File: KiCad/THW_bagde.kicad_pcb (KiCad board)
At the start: 2 copper layers, 84.9 x 82.9 mm, 46 parts, among them J1 USB_B, J2 ISP, SW1 SW_Push, SW2 SW_Push, SW3 SW_Push, U1 ATmega328-P, Y1 Crystal

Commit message: first tests with tks-badge firmware
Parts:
- added C8: 100n, Capacitor_THT:C_Disc_D3.8mm_W2.6mm_P2.50mm, F.Cu at (158.2, 88.5)
- C3: value C -> 100n
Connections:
- R10 pad 1: /PC5 -> /PC4
- R6 pad 1: /PC1 -> /PC0
- R7 pad 1: /PC2 -> /PC1
- R8 pad 1: /PC3 -> /PC2
- R9 pad 1: /PC4 -> /PC3
- U1 pad 23: unconnected-(U1-Pad23) -> /PC0
- U1 pad 28: /PC5 -> unconnected-(U1-Pad28)
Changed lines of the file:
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@@
   (net 22 "/PC3")
   (net 23 "/PC4")
-  (net 24 "/PC5")
+  (net 24 "Net-(C6-Pad1)")
   (net 25 "unconnected-(U1-Pad11)")
   (net 26 "+5V")
@@
   (net 31 "unconnected-(U1-Pad16)")
   (net 32 "unconnected-(U1-Pad21)")
-  (net 33 "unconnected-(U1-Pad23)")
+  (net 33 "Net-(C7-Pad1)")
   (net 34 "Net-(F1-Pad1)")
-  (net 35 "Net-(SW3-Pad2)")
-  (net 36 "Net-(SW2-Pad2)")
+  (net 35 "/PC0")
+  (net 36 "unconnected-(U1-Pad28)")
   (net 37 "GND")
   (net 38 "/RES")
@@
       (net 37 "GND") (pintype "passive"))
     (pad "2" thru_hole oval (at 10.16 0) (size 1.6 1.6) (drill 0.8) (layers *.Cu *.Mask)
-      (net 36 "Net-(SW2-Pad2)") (pintype "passive"))
+      (net 24 "Net-(C6-Pad1)") (pintype "passive"))
     (model "${KICAD6_3DMODEL_DIR}/Resistor_THT.3dshapes/R_Axial_DIN0207_L6.3mm_D2.5mm_P10.16mm_Horizontal.wrl"
       (offset (xyz 0 0 0))
@@
     (fp_line (start 8.23 1.25) (end 8.23 -1.25) (layer "F.Fab") (width 0.1))
     (pad "1" thru_hole circle (at 0 0) (size 1.6 1.6) (drill 0.8) (layers *.Cu *.Mask)
-      (net 24 "/PC5") (pintype "passive"))
+      (net 23 "/PC4") (pintype "passive"))
     (pad "2" thru_hole oval (at 10.16 0) (size 1.6 1.6) (drill 0.8) (layers *.Cu *.Mask)
       (net 12 "Net-(D10-Pad2)") (pintype "passive"))
@@
       (net 37 "GND") (pintype "passive"))
     (pad "2" thru_hole oval (at 10.16 0) (size 1.6 1.6) (drill 0.8) (layers *.Cu *.Mask)
-      (net 35 "Net-(SW3-Pad2)") (pintype "passive"))
+      (net 33 "Net-(C7-Pad1)") (pintype "passive"))
     (model "${KICAD6_3DMODEL_DIR}/Resistor_THT.3dshapes/R_Axial_DIN0207_L6.3mm_D2.5mm_P10.16mm_Horizontal.wrl"
       (offset (xyz 0 0 0))
@@
     (fp_line (start 1.93 -1.25) (end 1.93 1.25) (layer "F.Fab") (width 0.1))
     (pad "1" thru_hole circle (at 0 0) (size 1.6 1.6) (drill 0.8) (layers *.Cu *.Mask)
-      (net 19 "/PC2") (pintype "passive"))
+      (net 18 "/PC1") (pintype "passive"))
     (pad "2" thru_hole oval (at 10.16 0) (size 1.6 1.6) (drill 0.8) (layers *.Cu *.Mask)
       (net 9 "Net-(D7-Pad2)") (pintype "passive"))
@@
       (net 26 "+5V") (pinfunction "1") (pintype "passive"))
     (pad "2" thru_hole circle (at 6.5 4.5 90) (size 2 2) (drill 1.1) (layers *.Cu *.Mask)
-      (net 35 "Net-(SW3-Pad2)") (pinfunction "2") (pintype "passive"))
+      (net 33 "Net-(C7-Pad1)") (pinfunction "2") (pintype "passive"))
     (pad "2" thru_hole circle (at 0 4.5 90) (size 2 2) (drill 1.1) (layers *.Cu *.Mask)
-      (net 35 "Net-(SW3-Pad2)") (pinfunction "2") (pintype "passive"))
+      (net 33 "Net-(C7-Pad1)") (pinfunction "2") (pintype "passive"))
     (model "${KICAD6_3DMODEL_DIR}/Button_Switch_THT.3dshapes/SW_PUSH_6mm.wrl"
       (offset (xyz 0 0 0))
@@
     (fp_line (start 8.23 -1.25) (end 1.93 -1.25) (layer "F.Fab") (width 0.1))
     (pad "1" thru_hole circle (at 0 0) (size 1.6 1.6) (drill 0.8) (layers *.Cu *.Mask)
-      (net 22 "/PC3") (pintype "passive"))
+      (net 19 "/PC2") (pintype "passive"))
     (pad "2" thru_hole oval (at 10.16 0) (size 1.6 1.6) (drill 0.8) (layers *.Cu *.Mask)
       (net 10 "Net-(D8-Pad2)") (pintype "passive"))
@@
     (fp_line (start -0.65 -1.3) (end -0.65 1.3) (layer "F.Fab") (width 0.1))
     (pad "1" thru_hole circle (at 0 0 270) (size 1.6 1.6) (drill 0.8) (layers *.Cu *.Mask)
-      (net 36 "Net-(SW2-Pad2)") (pintype "passive"))
+      (net 24 "Net-(C6-Pad1)") (pintype "passive"))
     (pad "2" thru_hole circle (at 2.5 0 270) (size 1.6 1.6) (drill 0.8) (layers *.Cu *.Mask)
       (net 37 "GND") (pintype "passive"))
@@
     (fp_line (start 0 0) (end 1.93 0) (layer "F.Fab") (width 0.1))
     (pad "1" thru_hole circle (at 0 0) (size 1.6 1.6) (drill 0.8) (layers *.Cu *.Mask)
-      (net 18 "/PC1") (pintype "passive"))
+      (net 35 "/PC0") (pintype "passive"))
     (pad "2" thru_hole oval (at 10.16 0) (size 1.6 1.6) (drill 0.8) (layers *.Cu *.Mask)
       (net 8 "Net-(D6-Pad2)") (pintype "passive"))
@@
   )
   (footprint "Capacitor_THT:C_Disc_D3.8mm_W2.6mm_P2.50mm" (layer "F.Cu")
+    (at 158.25 88.45 -90)
+    (descr "C, Disc series, Radial, pin pitch=2.50mm, , diameter*width=3.8*2.6mm^2, Capacitor, http://www.vishay.com/docs/45233/krseries.pdf")
+    (tags "C Disc series Radial pin pitch 2.50mm  diameter 3.8mm width 2.6mm Capacitor")
+    (property "Sheetfile" "THW_bagde.kicad_sch")
+    (property "Sheetname" "")
+    (attr through_hole)
+    (fp_text reference "C8" (at 4.3 0 180) (layer "F.SilkS")
+      (effects (font (size 1 1) (thickness 0.15)))
+    )
+    (fp_text value "100n" (at 1.25 2.55 90) (layer "F.Fab") hide
+      (effects (font (size 1 1) (thickness 0.15)))
+    )
+    (fp_text user "${REFERENCE}" (at 1.25 0 90) (layer "F.Fab") hide
+      (effects (font (size 0.76 0.76) (thickness 0.114)))
+    )
+    (fp_line (start -0.77 0.795) (end -0.77 1.42) (layer "F.SilkS") (width 0.12))
+    (fp_line (start 3.27 0.795) (end 3.27 1.42) (layer "F.SilkS") (width 0.12))
+    (fp_line (start -0.77 -1.42) (end 3.27 -1.42) (layer "F.SilkS") (width 0.12))
+    (fp_line (start -0.77 -1.42) (end -0.77 -0.795) (layer "F.SilkS") (width 0.12))
+    (fp_line (start -0.77 1.42) (end 3.27 1.42) (layer "F.SilkS") (width 0.12))
+    (fp_line (start 3.27 -1.42) (end 3.27 -0.795) (layer "F.SilkS") (width 0.12))
+    (fp_line (start 3.55 -1.55) (end -1.05 -1.55) (layer "F.CrtYd") (width 0.05))
+    (fp_line (start -1.05 -1.55) (end -1.05 1.55) (layer "F.CrtYd") (width 0.05))
+    (fp_line (start -1.05 1.55) (end 3.55 1.55) (layer "F.CrtYd") (width 0.05))
+    (fp_line (start 3.55 1.55) (end 3.55 -1.55) (layer "F.CrtYd") (width 0.05))
+    (fp_line (start 3.15 1.3) (end 3.15 -1.3) (layer "F.Fab") (width 0.1))
+    (fp_line (start -0.65 -1.3) (end -0.65 1.3) (layer "F.Fab") (width 0.1))
+    (fp_line (start 3.15 -1.3) (end -0.65 -1.3) (layer "F.Fab") (width 0.1))
+    (fp_line (start -0.65 1.3) (end 3.15 1.3) (layer "F.Fab") (width 0.1))
+    (pad "1" thru_hole circle (at 0 0 270) (size 1.6 1.6) (drill 0.8) (layers *.Cu *.Mask)
+      (net 26 "+5V") (pintype "passive"))
+    (pad "2" thru_hole circle (at 2.5 0 270) (size 1.6 1.6) (drill 0.8) (layers *.Cu *.Mask)
+      (net 37 "GND") (pintype "passive"))
+    (model "${KICAD6_3DMODEL_DIR}/Capacitor_THT.3dshapes/C_Disc_D3.8mm_W2.6mm_P2.50mm.wrl"
+      (offset (xyz 0 0 0))
+      (scale (xyz 1 1 1))
+      (rotate (xyz 0 0 0))
+    )
+  )
+  (footprint "Capacitor_THT:C_Disc_D3.8mm_W2.6mm_P2.50mm" (layer "F.Cu")
     (at 140.9246 87.503 180)
     (descr "C, Disc series, Radial, pin pitch=2.50mm, , diameter*width=3.8*2.6mm^2, Capacitor, http://www.vishay.com/docs/45233/krseries.pdf")
@@
       (effects (font (size 1 1) (thickness 0.15)))
     )
-    (fp_text value "C" (at 1.25 2.55) (layer "F.Fab") hide
+    (fp_text value "100n" (at 1.25 2.55) (layer "F.Fab") hide
       (effects (font (size 1 1) (thickness 0.15)))
     )
@@
       (net 37 "GND") (pinfunction "GND") (pintype "passive"))
     (pad "23" thru_hole oval (at 7.62 12.7) (size 1.6 1.6) (drill 0.8) (layers *.Cu *.Mask)
-      (net 33 "unconnected-(U1-Pad23)") (pinfunction "PC0") (pintype "bidirectional"))
+      (net 35 "/PC0") (pinfunction "PC0") (pintype "bidirectional"))
     (pad "24" thru_hole oval (at 7.62 10.16) (size 1.6 1.6) (drill 0.8) (layers *.Cu *.Mask)
       (net 18 "/PC1") (pinfunction "PC1") (pintype "bidirectional"))
@@
       (net 23 "/PC4") (pinfunction "PC4") (pintype "bidirectional"))
     (pad "28" thru_hole oval (at 7.62 0) (size 1.6 1.6) (drill 0.8) (layers *.Cu *.Mask)
-      (net 24 "/PC5") (pinfunction "PC5") (pintype "bidirectional"))
+      (net 36 "unconnected-(U1-Pad28)") (pinfunction "PC5") (pintype "bidirectional+no_connect"))
     (model "${KICAD6_3DMODEL_DIR}/Package_DIP.3dshapes/DIP-28_W7.62mm.wrl"
       (offset (xyz 0 0 4))
@@
     (fp_line (start -0.65 1.3) (end 3.15 1.3) (layer "F.Fab") (width 0.1))
     (pad "1" thru_hole circle (at 0 0 270) (size 1.6 1.6) (drill 0.8) (layers *.Cu *.Mask)
-      (net 35 "Net-(SW3-Pad2)") (pintype "passive"))
+      (net 33 "Net-(C7-Pad1)") (pintype "passive"))
     (pad "2" thru_hole circle (at 2.5 0 270) (size 1.6 1.6) (drill 0.8) (layers *.Cu *.Mask)
       (net 37 "GND") (pintype "passive"))
@@
       (net 26 "+5V") (pinfunction "1") (pintype "passive"))
     (pad "2" thru_hole circle (at 0 4.5 90) (size 2 2) (drill 1.1) (layers *.Cu *.Mask)
-      (net 36 "Net-(SW2-Pad2)") (pinfunction "2") (pintype "passive"))
+      (net 24 "Net-(C6-Pad1)") (pinfunction "2") (pintype "passive"))
     (pad "2" thru_hole circle (at 6.5 4.5 90) (size 2 2) (drill 1.1) (layers *.Cu *.Mask)
-      (net 36 "Net-(SW2-Pad2)") (pinfunction "2") (pintype "passive"))
+      (net 24 "Net-(C6-Pad1)") (pinfunction "2") (pintype "passive"))
     (model "${KICAD6_3DMODEL_DIR}/Button_Switch_THT.3dshapes/SW_PUSH_6mm.wrl"
       (offset (xyz 0 0 0))
@@
     (fp_line (start 0 0) (end 1.93 0) (layer "F.Fab") (width 0.1))
     (pad "1" thru_hole circle (at 0 0) (size 1.6 1.6) (drill 0.8) (layers *.Cu *.Mask)
-      (net 23 "/PC4") (pintype "passive"))
+      (net 22 "/PC3") (pintype "passive"))
     (pad "2" thru_hole oval (at 10.16 0) (size 1.6 1.6) (drill 0.8) (layers *.Cu *.Mask)
       (net 11 "Net-(D9-Pad2)") (pintype "passive"))

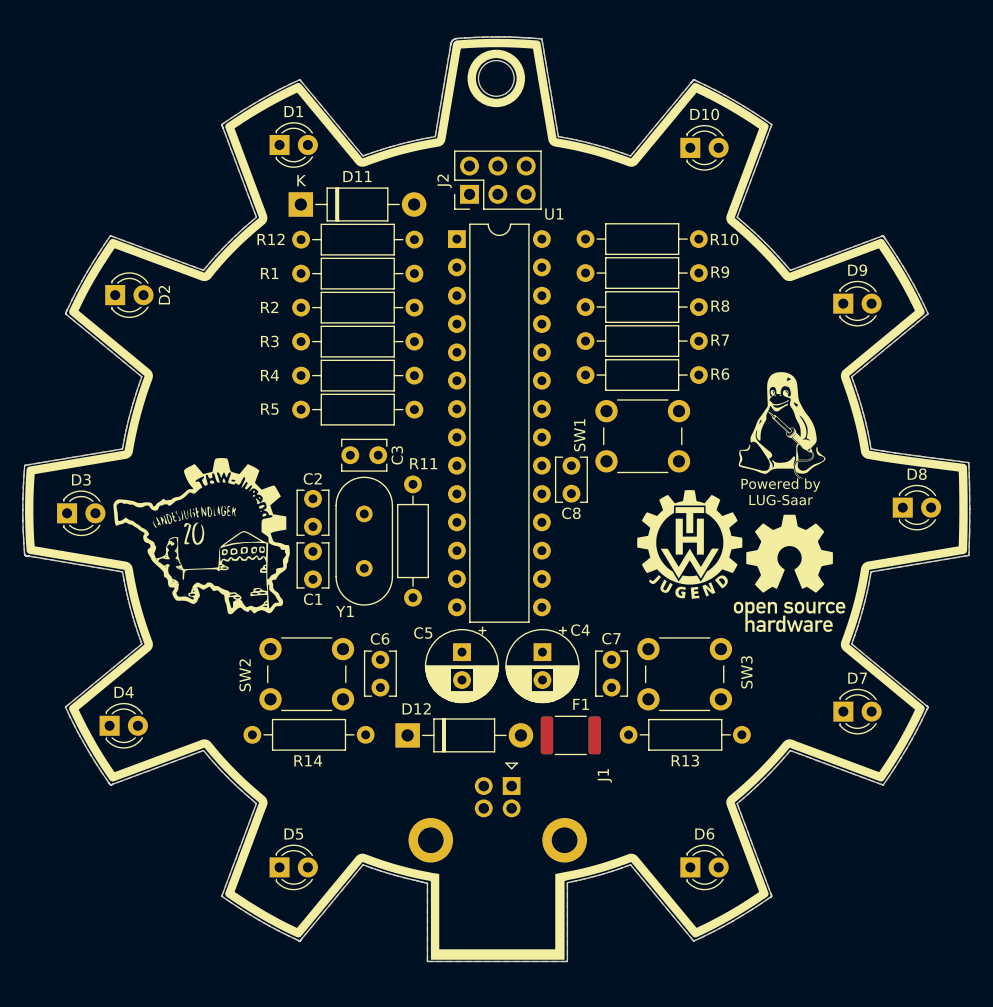
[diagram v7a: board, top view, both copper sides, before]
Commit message: fixing pin mapping
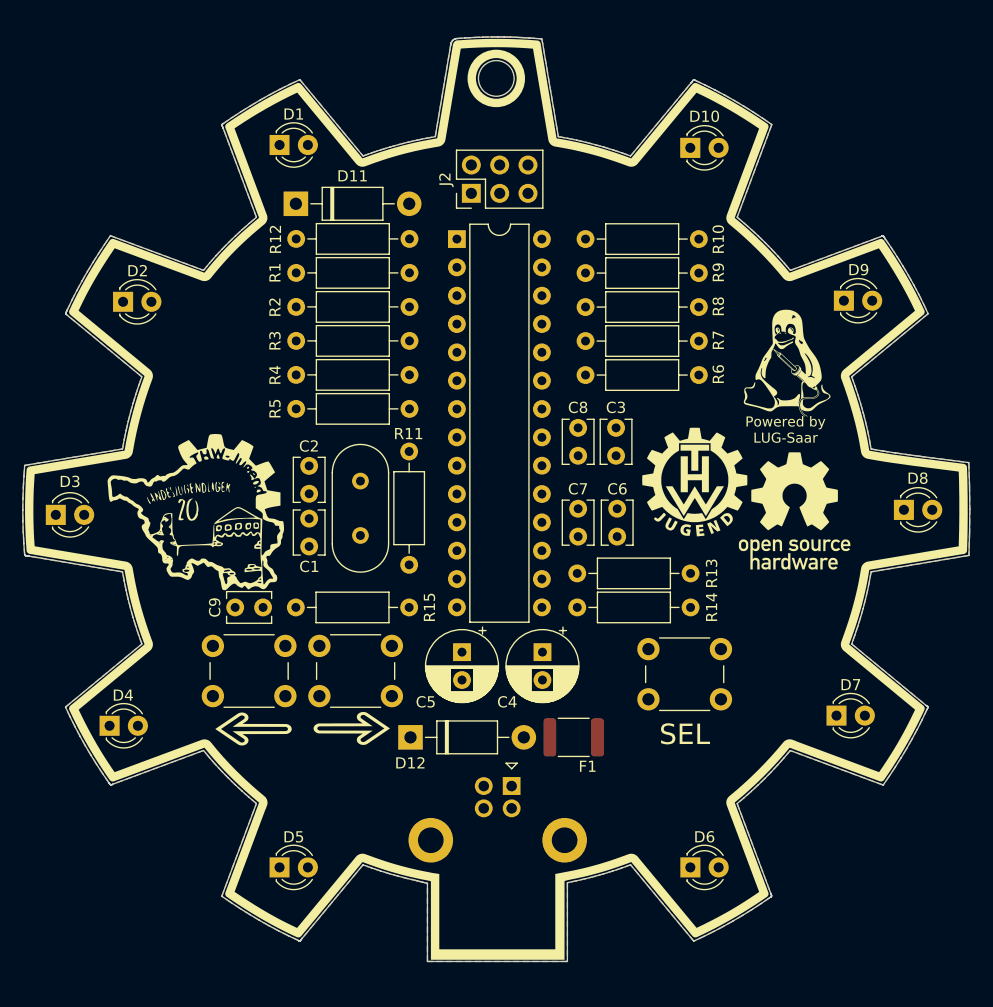
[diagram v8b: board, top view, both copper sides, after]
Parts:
- added C9: C, Capacitor_THT:C_Disc_D3.8mm_W2.6mm_P2.50mm, F.Cu at (128.1, 101.2)
- added G***: LOGO, LOGO, F.Cu at (129.8, 112.0)
- added G***: LOGO, LOGO, F.Cu at (138.5, 112.0)
- added R15: 10k, Resistor_THT:R_Axial_DIN0207_L6.3mm_D2.5mm_P10.16mm_Horizontal, F.Cu at (133.5, 101.2)
- moved SW1 41.1 mm to (126.1, 104.6)
- moved R14 40.9 mm to (168.9, 101.2), turned to 180 degrees
- moved C6 23.9 mm to (162.3, 94.8), turned to 90 degrees
- moved C3 21.3 mm to (162.2, 87.5), turned to 90 degrees
- moved R13 15.5 mm to (168.9, 98.1), turned to 180 degrees
- moved C7 11.4 mm to (158.8, 94.8), turned to 90 degrees
- moved G*** 5.61 mm to (169.3, 89.9)
- moved G*** 5.61 mm to (177.6, 77.6)
- moved G*** 5.61 mm to (178.2, 92.5)
- moved SW2 4.39 mm to (135.7, 104.6)
- moved C1 2.97 mm to (134.7, 93.2)
- moved C2 2.97 mm to (134.7, 91.0)
- moved R11 2.97 mm to (143.7, 97.3)
- moved Y1 2.97 mm to (139.3, 94.7)
- moved G*** 2.22 mm to (124.7, 91.8)
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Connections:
- C6 pad 1: Net-(C6-Pad1) -> /PB1
- C7 pad 1: Net-(C7-Pad1) -> /PB2
- R13 pad 2: Net-(C7-Pad1) -> /PB2
- R14 pad 2: Net-(C6-Pad1) -> /PB1
- SW1 pad 1: /RES -> +5V
- SW1 pad 2: GND -> /PB0
- SW2 pad 2: Net-(C6-Pad1) -> /PB1
- SW3 pad 2: Net-(C7-Pad1) -> /PB2
- U1 pad 14: unconnected-(U1-Pad14) -> /PB0
- U1 pad 15: unconnected-(U1-Pad15) -> /PB1
- U1 pad 16: unconnected-(U1-Pad16) -> /PB2
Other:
- board text added: "SEL"
